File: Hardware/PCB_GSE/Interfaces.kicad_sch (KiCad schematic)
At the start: 32 parts, among them J3 GT17HN-4DP-2H(D)(56), J4 Screw_Terminal_01x06, J5 Conn_02x10_Top_Bottom, J6 Conn_01x02, U5 SI5442DU-T1-GE3, U6 SI5442DU-T1-GE3, U7 SI5442DU-T1-GE3, U8 ISOW1044

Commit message: wip: begining layout
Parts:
- renumbered J4 to J3, J3 to J4, R25 to R28, R26 to R29, R27 to R30, R28 to R31, R29 to R32, R30 to R33, R31 to R34, R32 to R35

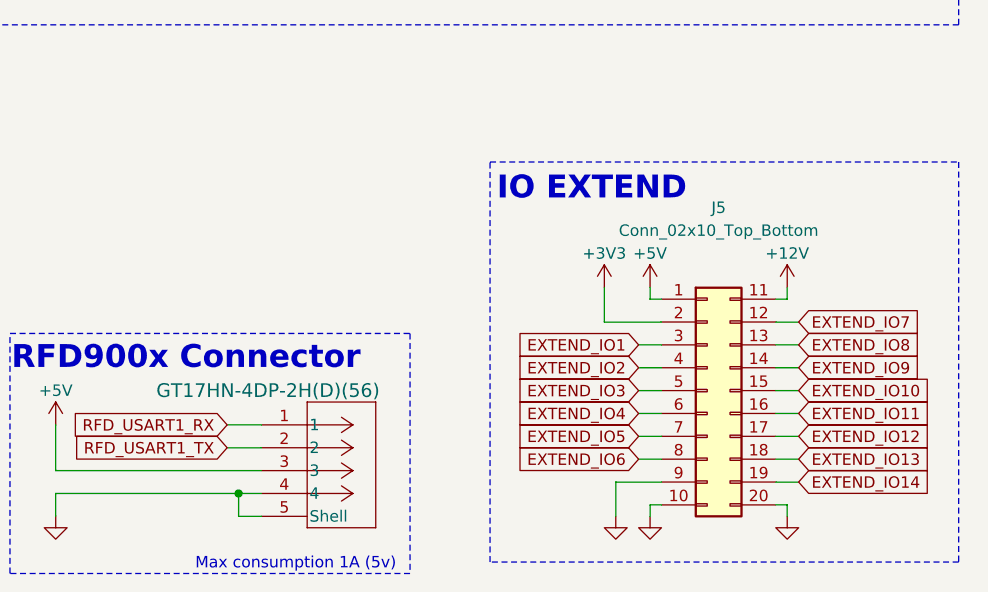
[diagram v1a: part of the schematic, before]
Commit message: feat: add 8MHz crystal, fix extended ios, fix pinout with HSE, update smt32 project, begin layout edge
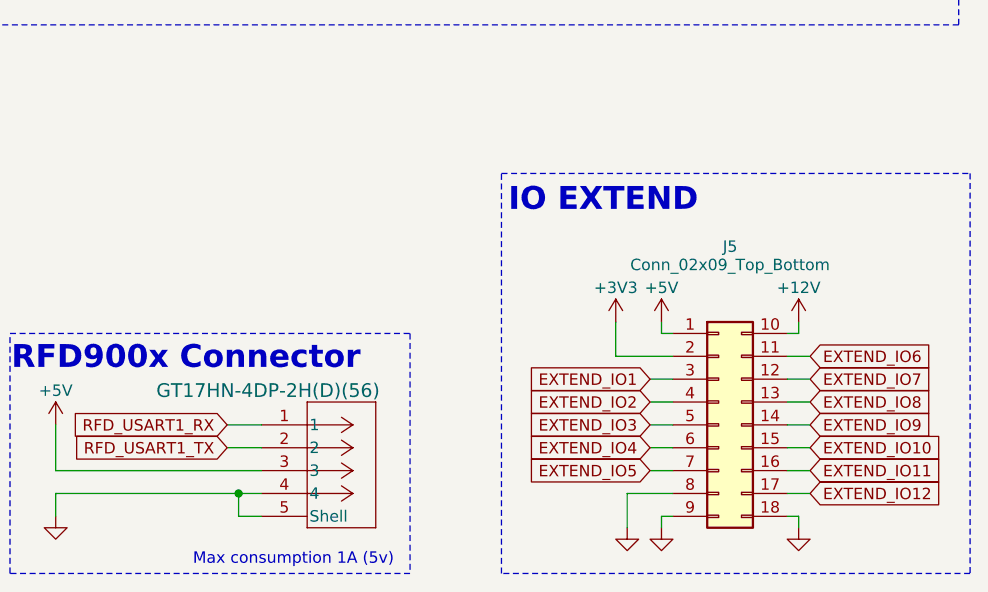
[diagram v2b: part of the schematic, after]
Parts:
- removed J5: Conn_02x10_Top_Bottom, Connector_PinHeader_2.54mm:PinHeader_2x10_P2.54mm_Vertical, symbol Connector_Generic:Conn_02x10_Top_Bottom
- added J5: Conn_02x09_Top_Bottom, Connector_PinHeader_2.54mm:PinHeader_2x09_P2.54mm_Vertical, symbol Connector_Generic:Conn_02x09_Top_Bottom
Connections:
- net +12V: now also J5.10 (Pin_10)
- net +3V3: now also J5.2 (Pin_2)
- net +5V: now also J5.1 (Pin_1)
- net EXTEND_IO1: now also J5.3 (Pin_3)
- net EXTEND_IO10: now also J5.15 (Pin_15)
- net EXTEND_IO11: now also J5.16 (Pin_16)
- net EXTEND_IO12: now also J5.17 (Pin_17)
- net EXTEND_IO2: now also J5.4 (Pin_4)
- net EXTEND_IO3: now also J5.5 (Pin_5)
- net EXTEND_IO4: now also J5.6 (Pin_6)
- net EXTEND_IO5: now also J5.7 (Pin_7)
- net EXTEND_IO6: now also J5.11 (Pin_11)
- net EXTEND_IO7: now also J5.12 (Pin_12)
- net EXTEND_IO8: now also J5.13 (Pin_13)
- net EXTEND_IO9: now also J5.14 (Pin_14)
- net GND: now also J5.18 (Pin_18), J5.8 (Pin_8), J5.9 (Pin_9)

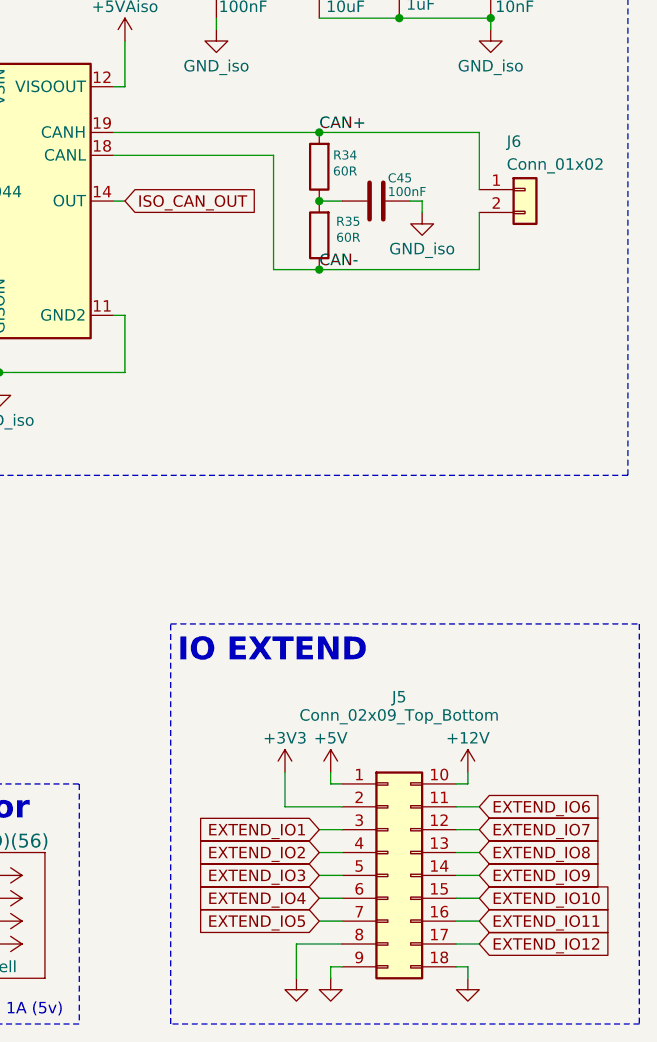
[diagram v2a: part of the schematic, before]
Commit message: wip : add BOM for 12V buck-boost
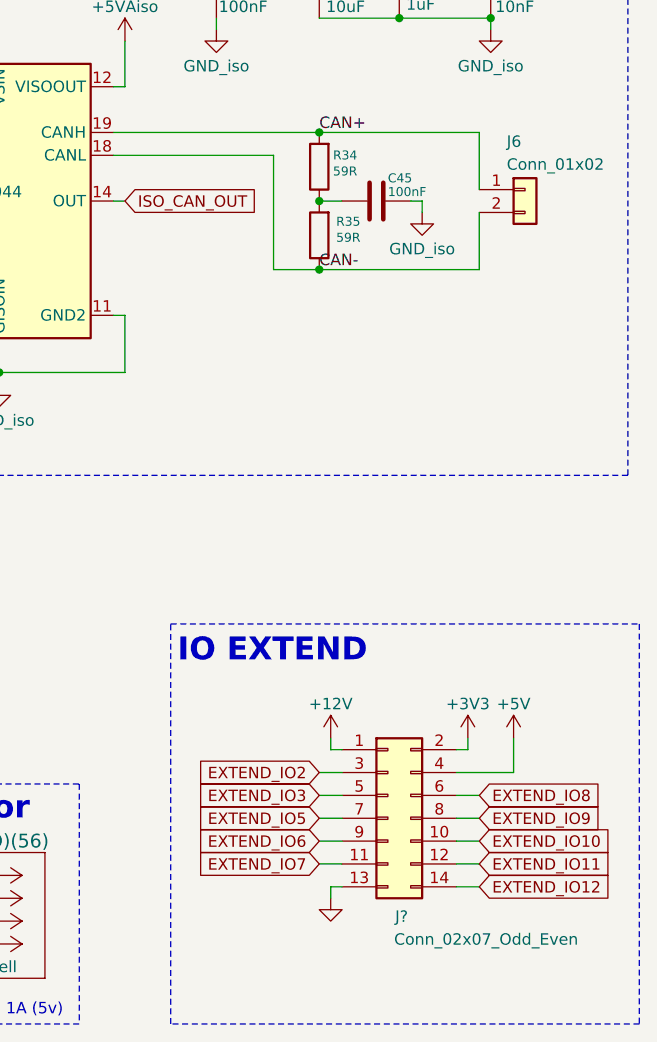
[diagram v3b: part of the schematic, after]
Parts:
- removed J5: Conn_02x09_Top_Bottom, Connector_PinHeader_2.54mm:PinHeader_2x09_P2.54mm_Vertical, symbol Connector_Generic:Conn_02x09_Top_Bottom
- added J?: Conn_02x07_Odd_Even, Connector_PinHeader_2.54mm:PinHeader_2x07_P2.54mm_Vertical, symbol Connector_Generic:Conn_02x07_Odd_Even
- R34, R35: value 60R -> 59R; DigiKey_Part_Number (none) -> 311-59.0CRCT-ND; Manufacturer_Part_Number (none) -> RC0805FR-0759RL
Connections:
- net +12V: now also J?.1 (Pin_1)
- net +3V3: now also J?.2 (Pin_2)
- net +5V: now also J?.4 (Pin_4)
- net EXTEND_IO10: now also J?.10 (Pin_10)
- net EXTEND_IO11: now also J?.12 (Pin_12)
- net EXTEND_IO12: now also J?.14 (Pin_14)
- net EXTEND_IO2: now also J?.3 (Pin_3)
- net EXTEND_IO3: now also J?.5 (Pin_5)
- net EXTEND_IO5: now also J?.7 (Pin_7)
- net EXTEND_IO6: now also J?.9 (Pin_9)
- net EXTEND_IO7: now also J?.11 (Pin_11)
- net EXTEND_IO8: now also J?.6 (Pin_6)
- net EXTEND_IO9: now also J?.8 (Pin_8)
- net GND: now also J?.13 (Pin_13)

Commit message: wip : subsystems layout
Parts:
- gave numbers to parts that had none: 1
- renumbered C36 to C45, C37 to C46, C38 to C47, C39 to C48, C40 to C49, C41 to C50, C42 to C51, C43 to C52, C44 to C53, C45 to C54, C46 to C55, C47 to C56, D2 to D1, D3 to D2, D4 to D3, R28 to R36, R29 to R37, R30 to R38, R31 to R39, R32 to R40, R33 to R41, R34 to R42, R35 to R43

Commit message: wip : routing local circuits and power planes
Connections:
- net ISO_CAN_OUT: no longer names the net of U8.14 (OUT)
- no-connect marks 2 -> 3
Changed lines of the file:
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@@
+	)
+	(no_connect
+		(at 226.06 73.66)
 	)
 	(no_connect
@@
 		(pts
 			(xy 50.8 45.72) (xy 50.8 48.26)
-		)
-		(stroke
-			(width 0)
-			(type default)
-		)
-	)
-	(wire
-		(pts
-			(xy 227.33 73.66) (xy 226.06 73.66)
 		)
 		(stroke
@@
 			(effects
 				(font
-					(size 1.27 1.27)
-				)
-				(justify left)
-				(hide yes)
-			)
-		)
-	)
-	(global_label "ISO_CAN_OUT"
-		(shape input)
-		(at 227.33 73.66 0)
-		(fields_autoplaced yes)
-		(effects
-			(font
-				(size 1.27 1.27)
-			)
-			(justify left)
-		)
-		(property "Intersheetrefs" "${INTERSHEET_REFS}"
-			(at 242.7129 73.66 0)
-			(effects
-				(font

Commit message: fix(gse & moteur): mapping + routing, remove CAN_ISO_IN/OUT
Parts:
- J5: now left out of the parts list
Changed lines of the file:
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@@
 		(unit 1)
 		(exclude_from_sim no)
-		(in_bom yes)
-		(on_board yes)
+		(in_bom no)
+		(on_board no)
 		(dnp no)
 		(property "Reference" "J5"

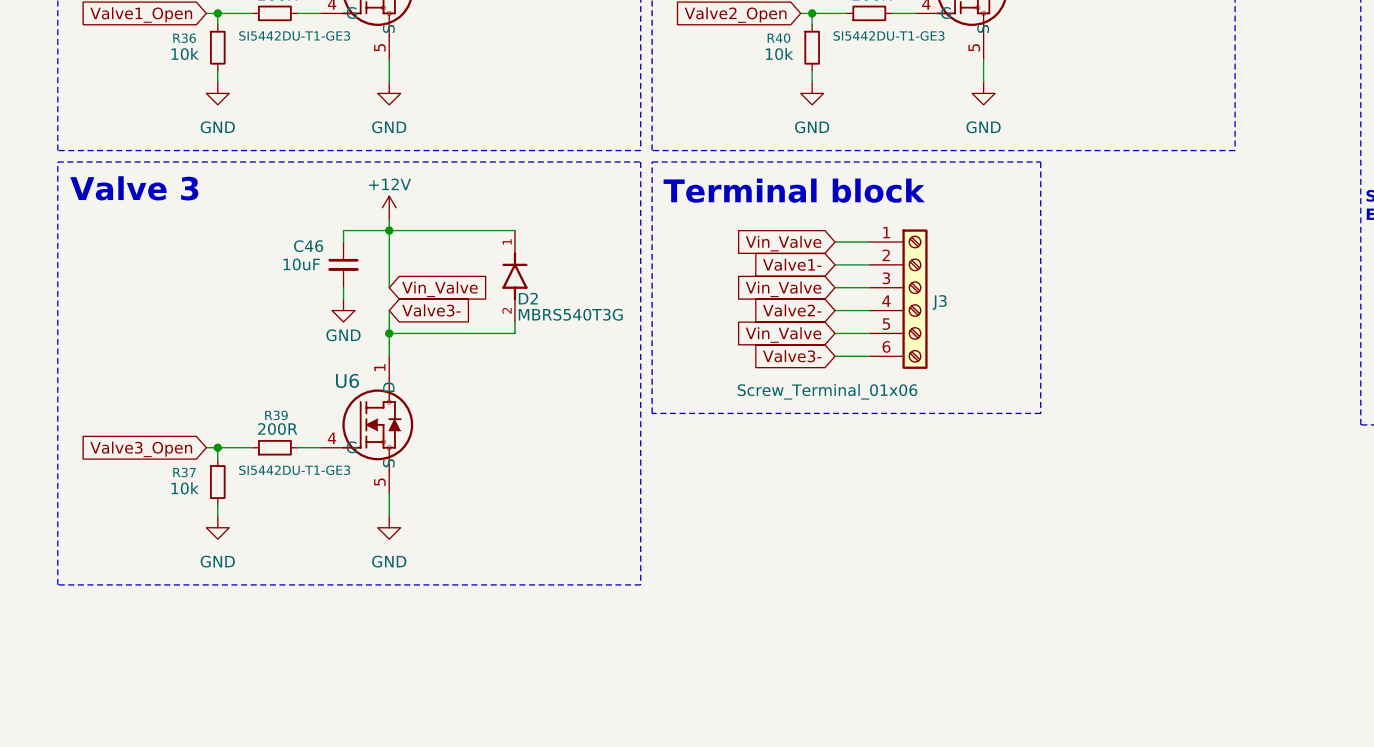
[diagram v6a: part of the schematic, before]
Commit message: fix : replace valve 3 with servomotor on schematic
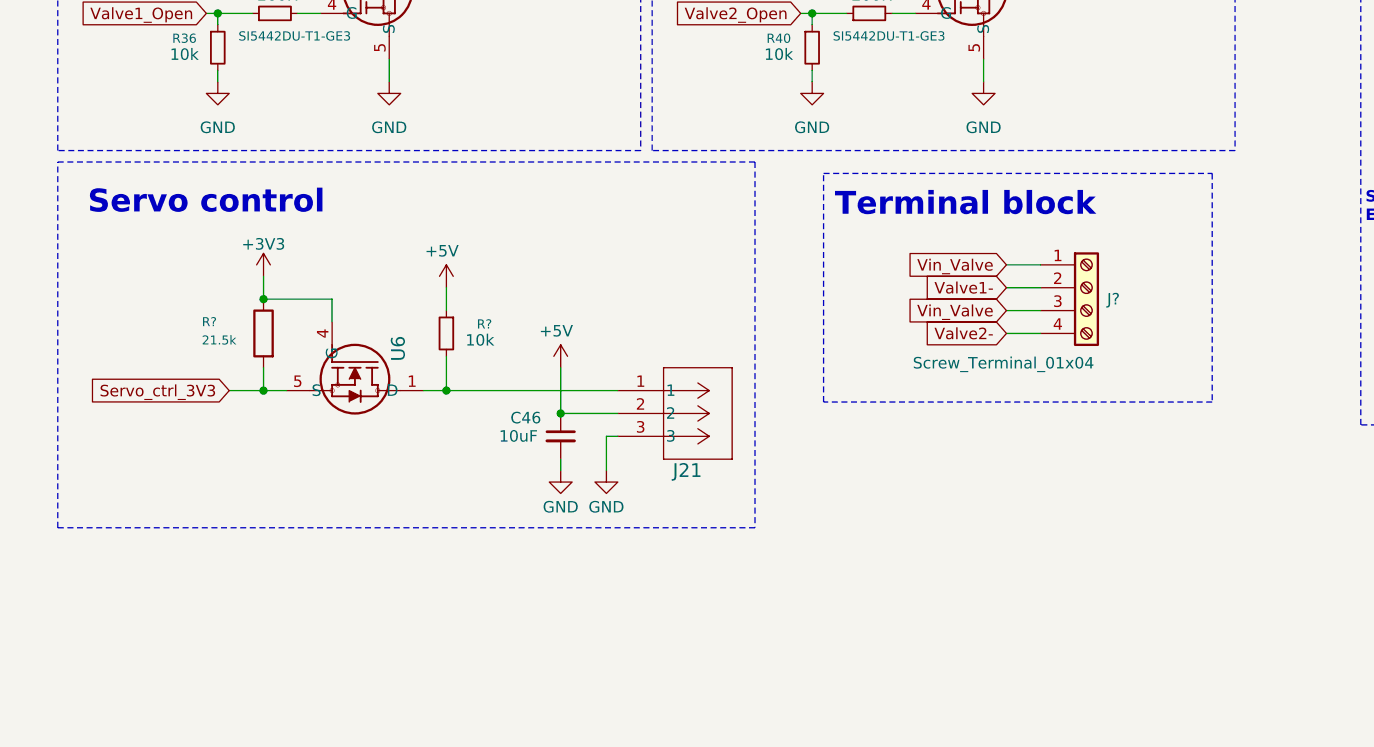
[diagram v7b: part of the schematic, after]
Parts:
- removed D2: MBRS540T3G, pcb_moteur:DIODE_SMB_2L_ONS, symbol PCB_GSE:MBRS540T3G
- removed J3: Screw_Terminal_01x06, pcb_moteur:CONN_1725698_PXC, symbol Connector:Screw_Terminal_01x06
- removed R37: 10k, Resistor_SMD:R_0805_2012Metric, symbol Device:R_Small
- removed R39: 200R, Resistor_SMD:R_0805_2012Metric, symbol Device:R_Small
- added J21: BM03B-GHS-TBT, pcb_moteur:CONN_BM03B-GHS-TBT_JST, symbol pcb_moteur:BM03B-GHS-TBT
- added J?: Screw_Terminal_01x04, pcb_moteur:CONN_OSTVN04A150_OST, symbol Connector:Screw_Terminal_01x04
- added R?: 10k, Resistor_SMD:R_0805_2012Metric, symbol Device:R_Small
- added R?: 21.5k, Resistor_SMD:R_0805_2012Metric, symbol Device:R
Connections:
- net +12V: now also J?.1 (Pin_1), J?.3 (Pin_3); no longer C46.1
- net +3V3: now also U6.4 (G), R?.1
- net +5V: now also C46.1, J21.2, R?.1
- net GND: now also J21.3; no longer U6.5 (S), U6.9 (S)
- net Valve1-: now also J?.2 (Pin_2)
- net Valve2-: now also J?.4 (Pin_4)
- net Valve3-: no longer names the net of U6.1 (D), U6.2 (D), U6.3 (D), U6.6 (D), U6.7 (D), U6.8 (D)
- net Valve3-: now also J21.1, R?.2
- new net Servo_ctrl_3V3: R?.2, U6.5 (S), U6.9 (S)
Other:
- note added: "Servo control"
- note removed: "Valve 3"
- moved on the sheet: C46, U6

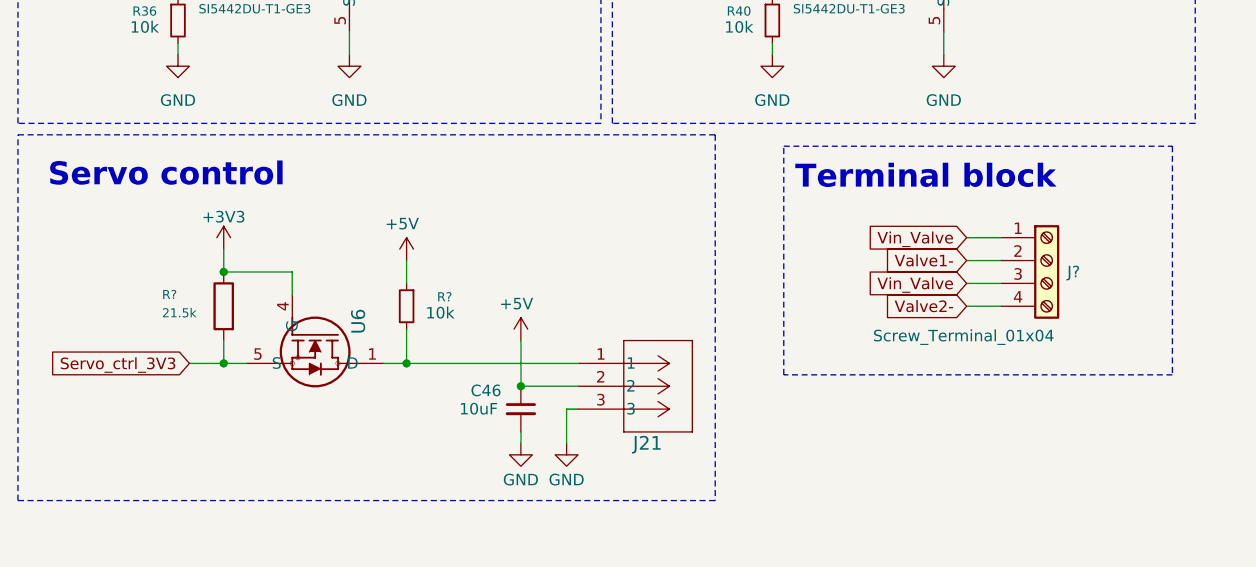
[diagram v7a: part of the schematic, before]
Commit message: fix : routing des modifications Servo et capteur pression
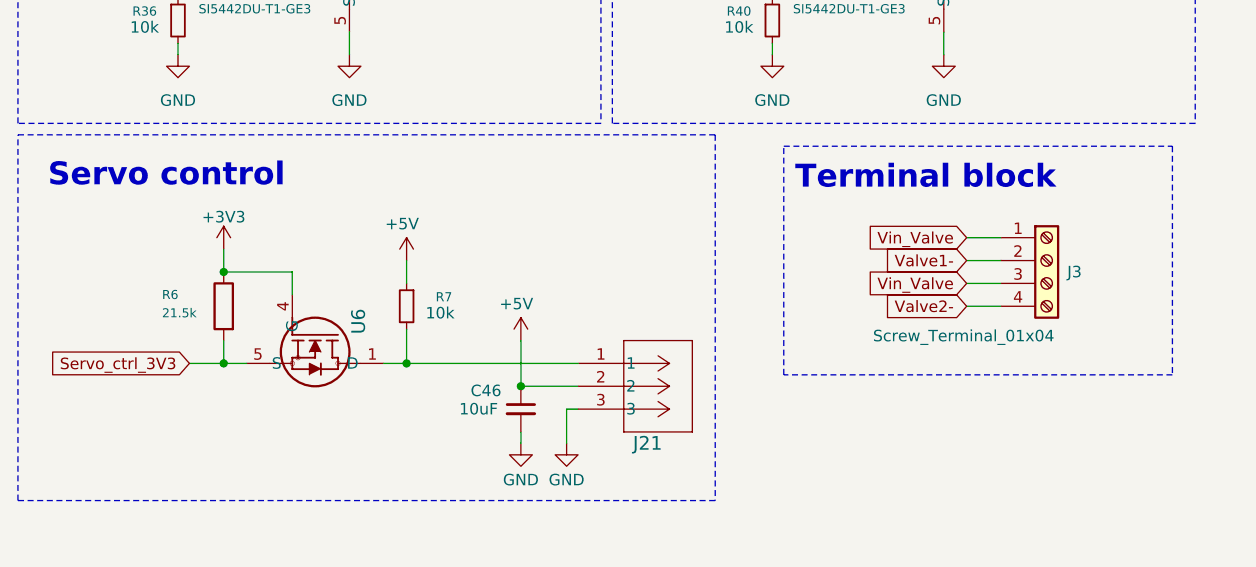
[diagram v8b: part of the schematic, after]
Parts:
- gave numbers to parts that had none: 3
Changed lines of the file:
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@@
 		(on_board yes)
 		(dnp no)
-		(property "Reference" "R?"
+		(property "Reference" "R7"
 			(at 62.23 92.964 0)
 			(effects
@@
 			(project "PCB_GSE"
 				(path "/a63f9ed4-21e4-42d0-8bfc-f96143f84d4d/3c37fe83-9ec5-4bf7-b24c-730d18a48e1f"
-					(reference "R?")
+					(reference "R7")
 					(unit 1)
 				)
@@
 		(on_board yes)
 		(dnp no)
-		(property "Reference" "R?"
+		(property "Reference" "R6"
 			(at 29.972 92.71 0)
 			(effects
@@
 			(project "PCB_GSE"
 				(path "/a63f9ed4-21e4-42d0-8bfc-f96143f84d4d/3c37fe83-9ec5-4bf7-b24c-730d18a48e1f"
-					(reference "R?")
+					(reference "R6")
 					(unit 1)
 				)
@@
 		(on_board yes)
 		(dnp no)
-		(property "Reference" "J?"
+		(property "Reference" "J3"
 			(at 130.556 90.17 0)
 			(effects
@@
 			(project "PCB_GSE"
 				(path "/a63f9ed4-21e4-42d0-8bfc-f96143f84d4d/3c37fe83-9ec5-4bf7-b24c-730d18a48e1f"
-					(reference "J?")
+					(reference "J3")
 					(unit 1)
 				)
